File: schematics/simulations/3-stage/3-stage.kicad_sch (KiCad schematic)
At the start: 43 parts, among them U1 AD8422ARMZ, U2 OPA2156xD, U3 OPA2156xD, U4 AD8422ARMZ, U5 OPA2156xD, U6 OPA2156xD, U7 AD8422ARMZ, U8 OPA2156xD, U9 OPA2156xD

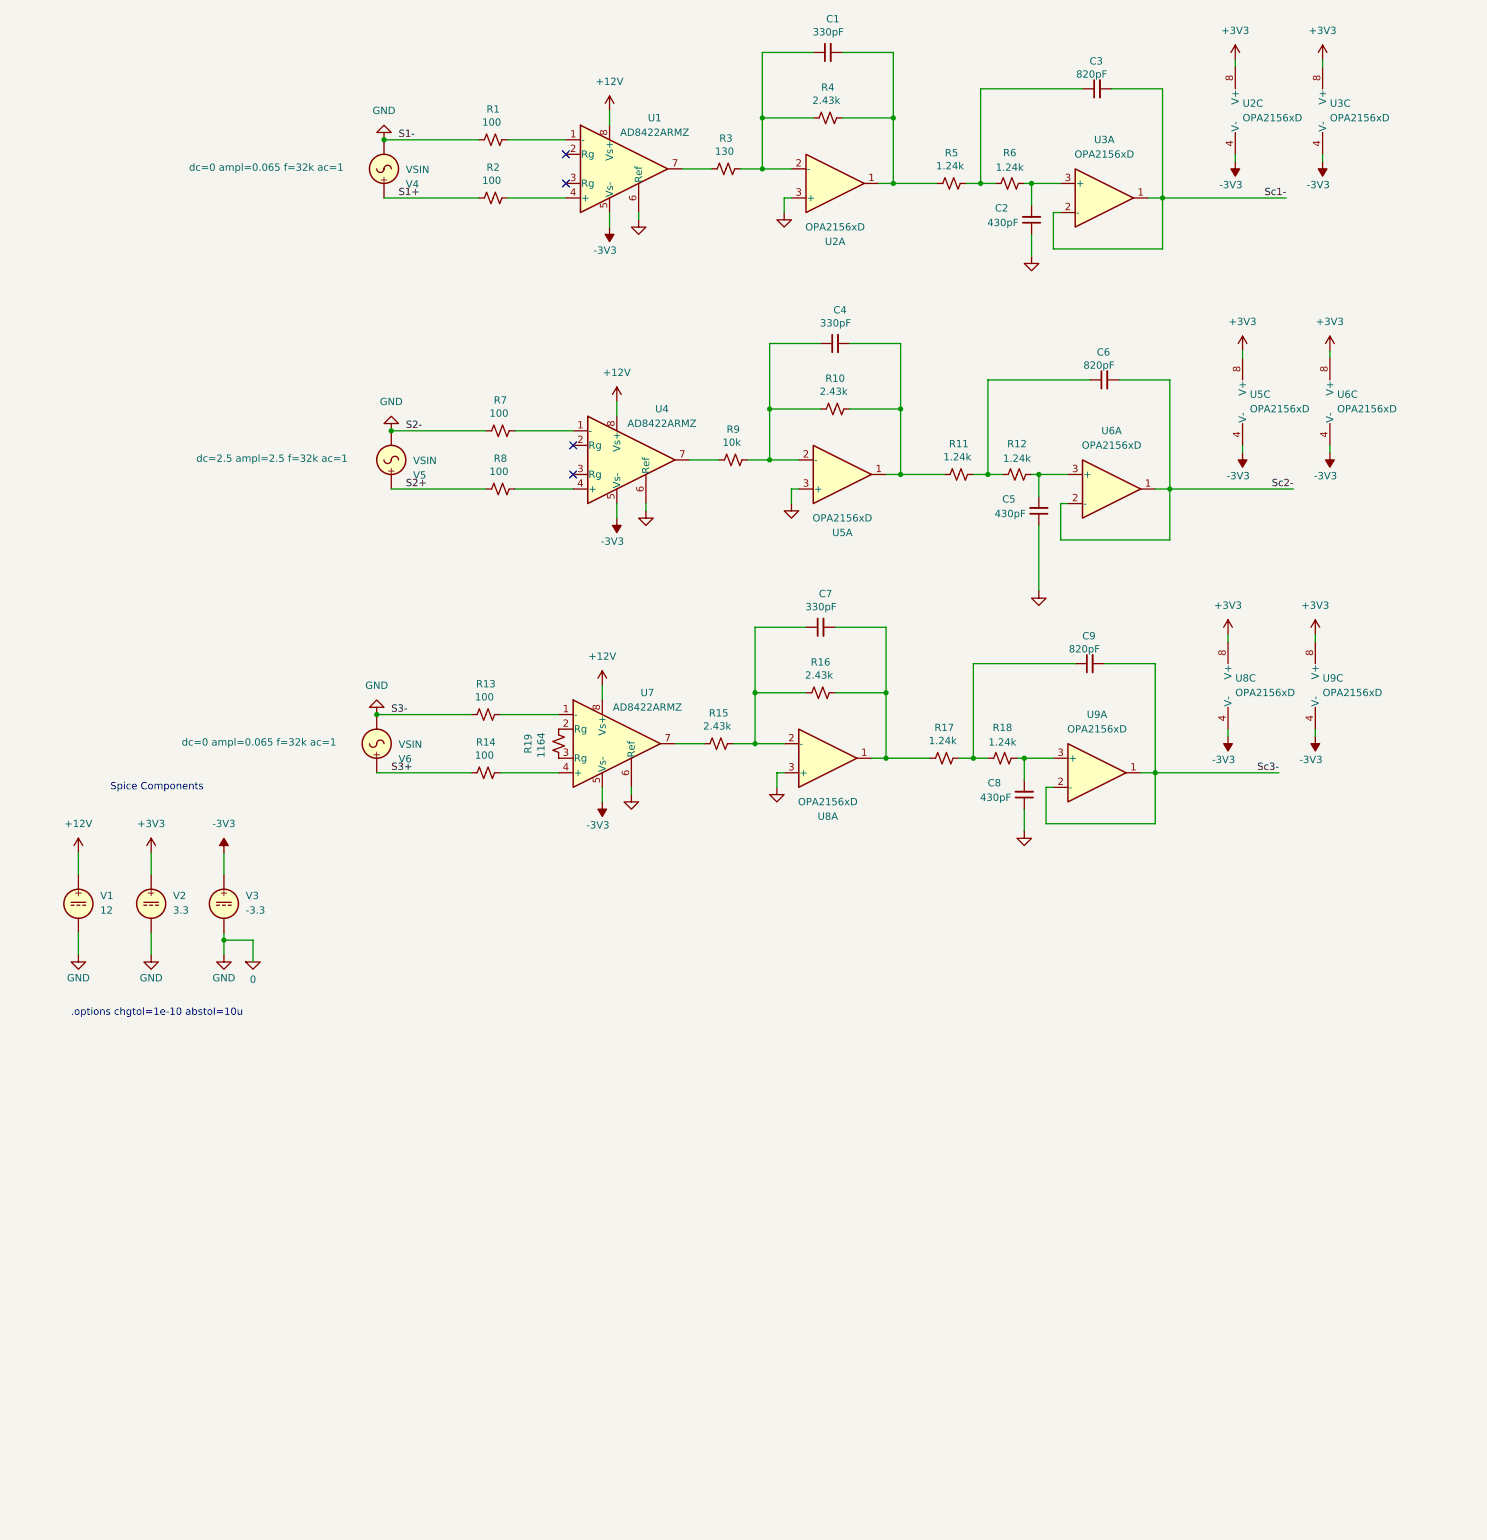
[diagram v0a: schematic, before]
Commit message: update(review):
1. Take gain resistor out of AFE filter
2. Breakout I2C
3. Move fuse to cover both 12V rails
4. Silkscreens
5. More testpoints + change to clip ons
6. Match ADC input max and filter output max
7. Add shunt for current resistors
8. Thermocouples
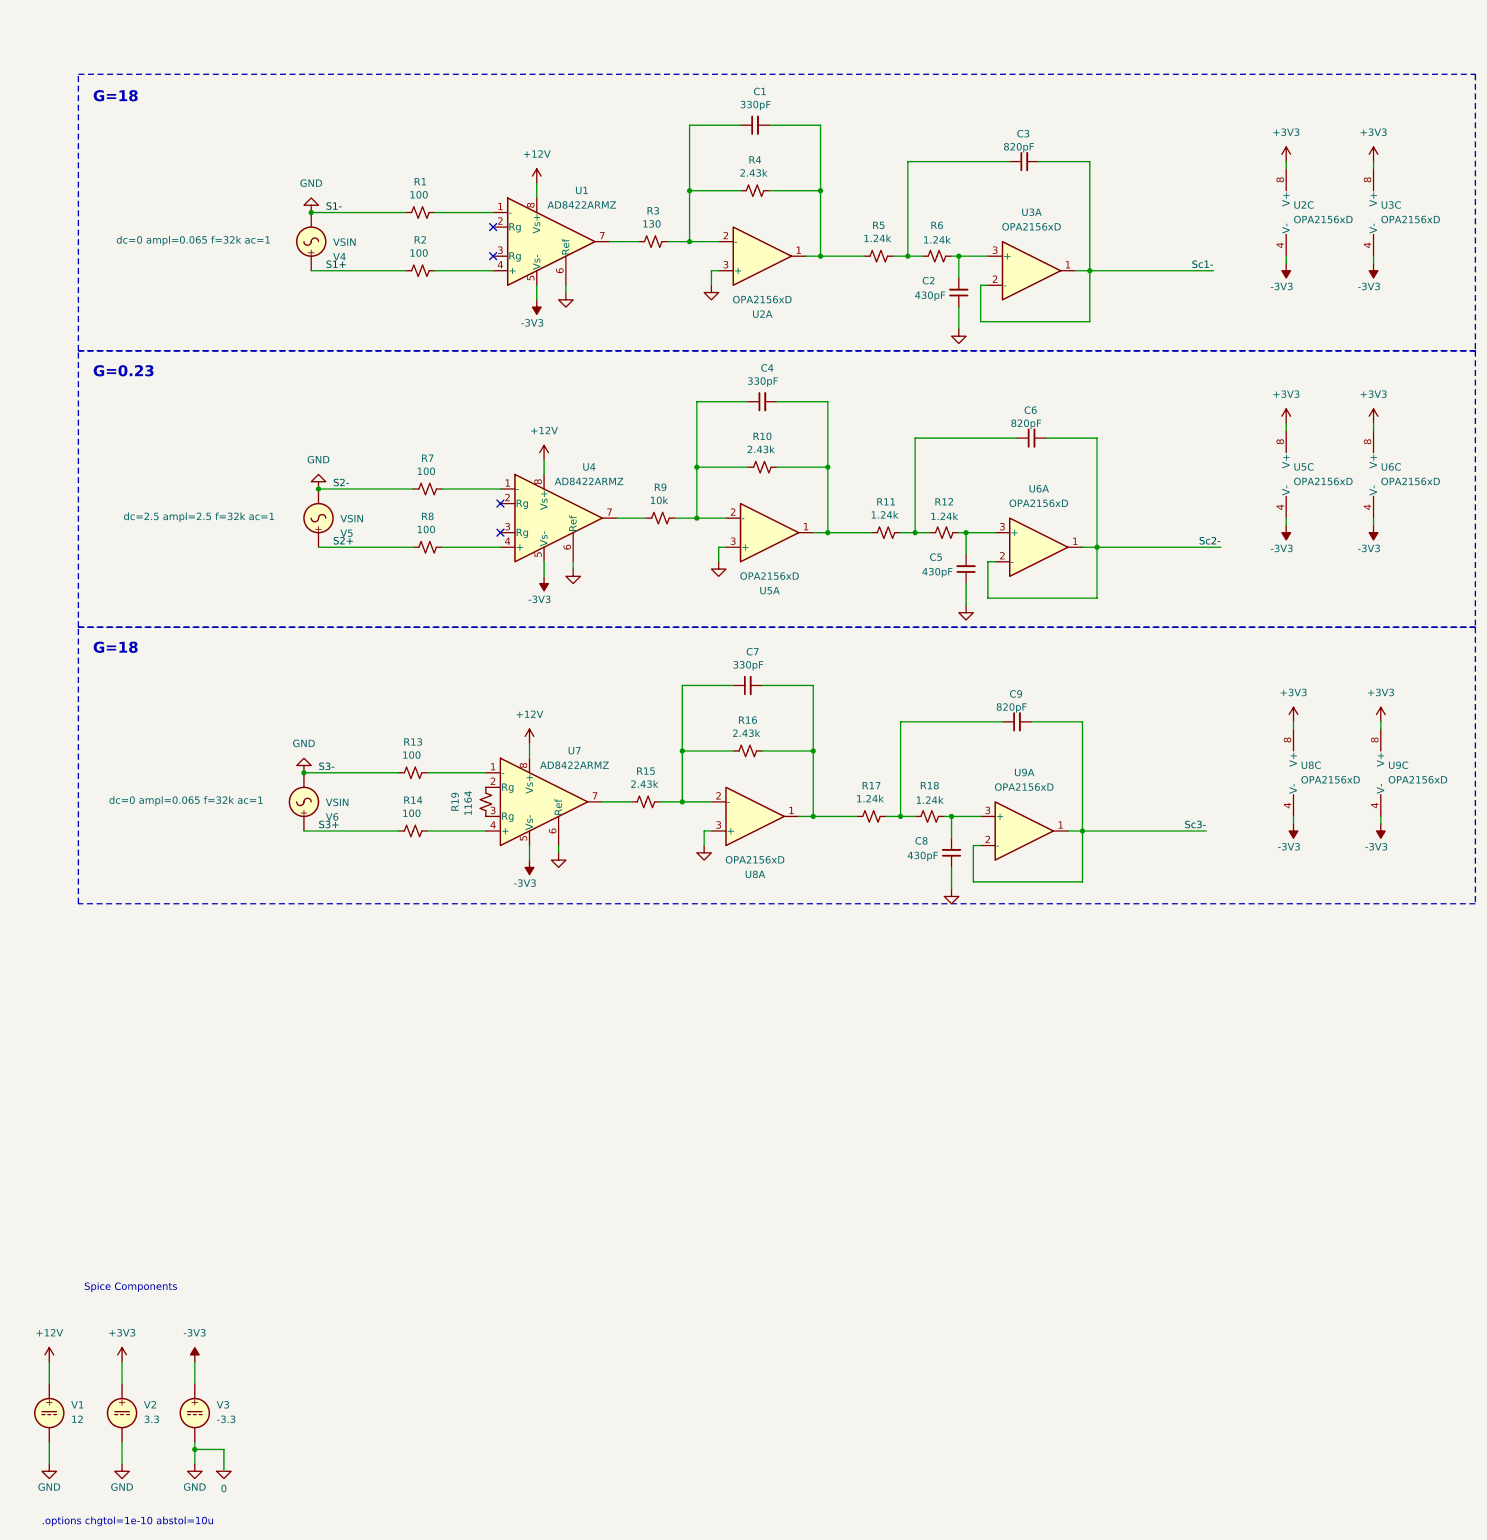
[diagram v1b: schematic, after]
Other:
- note added: "G=0.23"
- note added: "G=18"
- moved on the sheet: C1, C2, C3, C4, C5, C6, C7, C8, C9, R1, R10, R11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
